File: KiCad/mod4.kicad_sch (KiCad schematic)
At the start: 51 parts, among them M7 Fan_4pin, M8 Fan_4pin, U4 ZD25Q64BSIGT

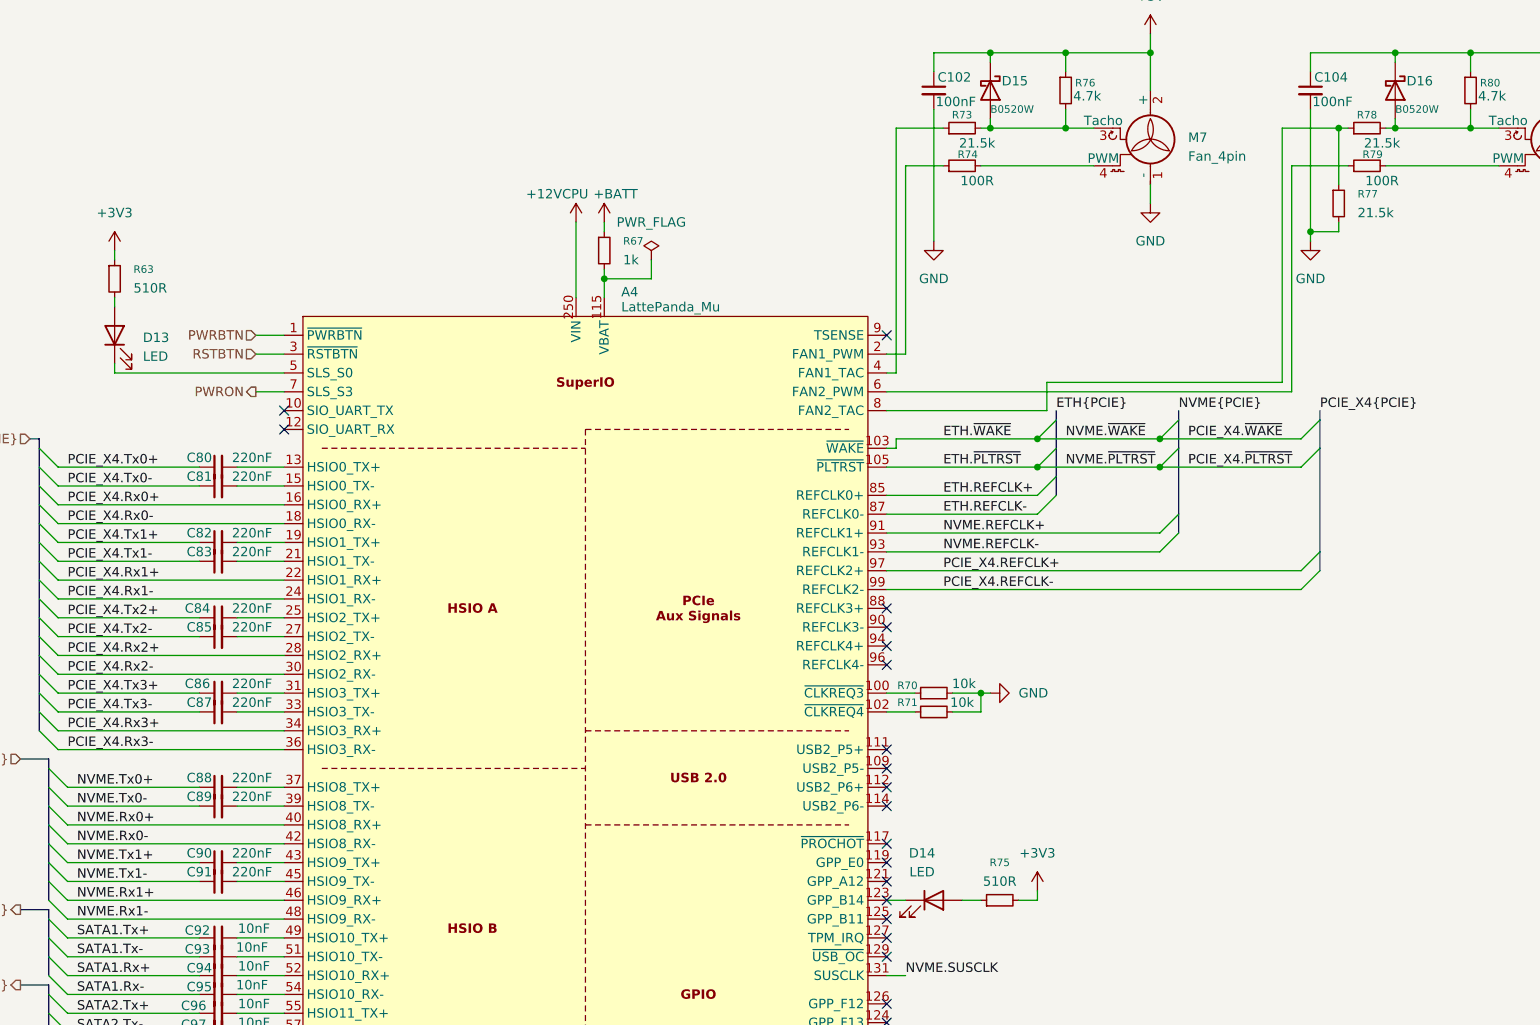
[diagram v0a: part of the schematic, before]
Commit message: Add most passive component footprints
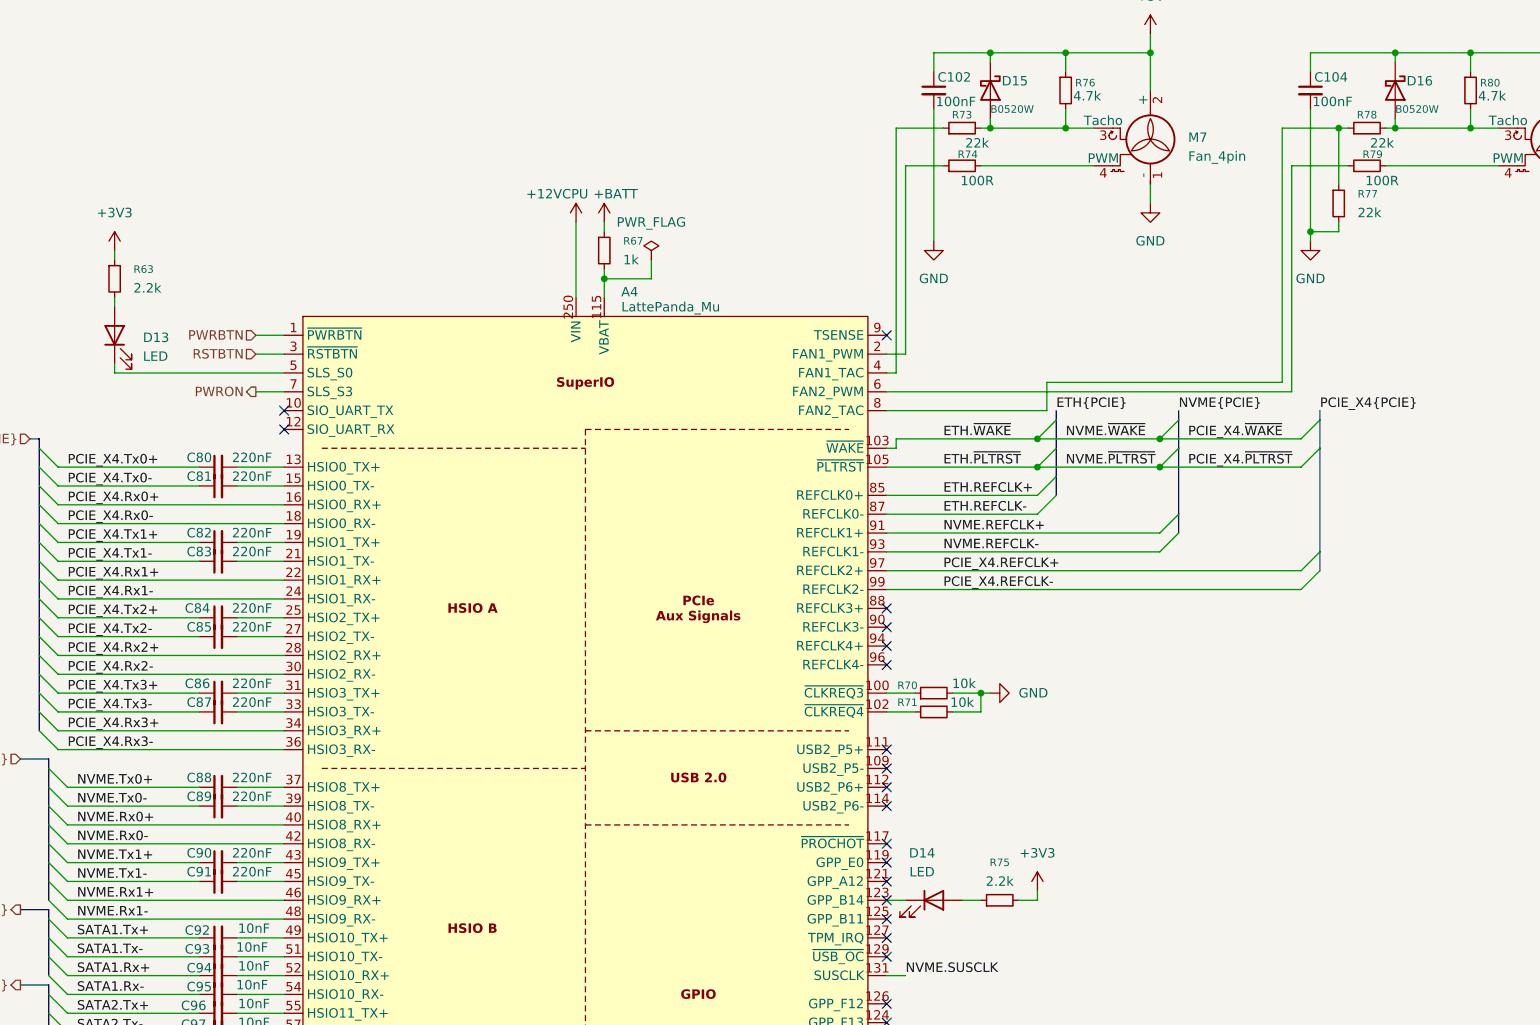
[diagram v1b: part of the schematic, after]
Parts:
- C100, C101, C102, C103, C104, C80, C81, C82, C83, C84, C85, C86, C87, C88, C89, C90, C91, C92, C93, C94, C95, C96, C97, C98, C99: footprint Capacitor_SMD:C_0603_1608Metric -> Capacitor_SMD:C_0402_1005Metric
- D13, D14: footprint (none) -> LED_SMD:LED_0603_1608Metric
- D15, D16: footprint (none) -> Diode_SMD:D_SOD-123
- M7, M8: footprint (none) -> Connector:FanPinHeader_1x04_P2.54mm_Vertical
- R63, R75: value 510R -> 2.2k; footprint (none) -> Resistor_SMD:R_0402_1005Metric
- R64, R65, R66, R68, R69, R70, R71, R72, R74, R76, R79, R80: footprint (none) -> Resistor_SMD:R_0402_1005Metric
- R67: footprint (none) -> Resistor_SMD:R_0805_2012Metric
- R73, R77, R78: value 21.5k -> 22k; footprint (none) -> Resistor_SMD:R_0402_1005Metric
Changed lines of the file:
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@@
 			)
 		)
-		(property "Footprint" "Capacitor_SMD:C_0603_1608Metric"
+		(property "Footprint" "Capacitor_SMD:C_0402_1005Metric"
 			(at 237.49 176.53 0)
 			(effects
@@
 			)
 		)
-		(property "Footprint" ""
+		(property "Footprint" "Resistor_SMD:R_0402_1005Metric"
 			(at 334.01 133.35 0)
 			(effects
@@
 			)
 		)
-		(property "Footprint" ""
+		(property "Footprint" "Resistor_SMD:R_0402_1005Metric"
 			(at 351.79 52.07 0)
 			(effects
@@
 			)
 		)
-		(property "Footprint" "Capacitor_SMD:C_0603_1608Metric"
+		(property "Footprint" "Capacitor_SMD:C_0402_1005Metric"
 			(at 237.49 181.61 0)
 			(effects
@@
 			)
 		)
-		(property "Footprint" ""
+		(property "Footprint" "Resistor_SMD:R_0402_1005Metric"
 			(at 237.49 232.41 0)
 			(effects
@@
 			)
 		)
-		(property "Value" "21.5k"
+		(property "Value" "22k"
 			(at 391.16 68.5799 0)
 			(effects
@@
 			)
 		)
-		(property "Footprint" ""
+		(property "Footprint" "Resistor_SMD:R_0402_1005Metric"
 			(at 388.62 67.31 0)
 			(effects
@@
 			)
 		)
-		(property "Footprint" "Capacitor_SMD:C_0603_1608Metric"
+		(property "Footprint" "Capacitor_SMD:C_0402_1005Metric"
 			(at 237.49 123.19 0)
 			(effects
@@
 			)
 		)
-		(property "Footprint" "Capacitor_SMD:C_0603_1608Metric"
+		(property "Footprint" "Capacitor_SMD:C_0402_1005Metric"
 			(at 237.49 115.57 0)
 			(effects
@@
 			)
 		)
-		(property "Footprint" ""
+		(property "Footprint" "Resistor_SMD:R_0402_1005Metric"
 			(at 406.4 52.07 0)
 			(effects
@@
 			)
 		)
-		(property "Value" "21.5k"
+		(property "Value" "22k"
 			(at 394.462 59.182 90)
 			(effects
@@
 			)
 		)
-		(property "Footprint" ""
+		(property "Footprint" "Resistor_SMD:R_0402_1005Metric"
 			(at 392.43 57.15 0)
 			(effects
@@
 			)
 		)
-		(property "Value" "21.5k"
+		(property "Value" "22k"
 			(at 339.852 59.182 90)
 			(effects
@@
 			)
 		)
-		(property "Footprint" ""
+		(property "Footprint" "Resistor_SMD:R_0402_1005Metric"
 			(at 337.82 57.15 0)
 			(effects
@@
 			)
 		)
-		(property "Footprint" "Capacitor_SMD:C_0603_1608Metric"
+		(property "Footprint" "Capacitor_SMD:C_0402_1005Metric"
 			(at 384.81 52.07 0)
 			(effects
@@
 			)
 		)
-		(property "Footprint" "Capacitor_SMD:C_0603_1608Metric"
+		(property "Footprint" "Capacitor_SMD:C_0402_1005Metric"
 			(at 237.49 168.91 0)
 			(effects
@@
 			)
 		)
-		(property "Footprint" "Capacitor_SMD:C_0603_1608Metric"
+		(property "Footprint" "Capacitor_SMD:C_0402_1005Metric"
 			(at 237.49 166.37 0)
 			(effects
@@
 			)
 		)
-		(property "Footprint" ""
+		(property "Footprint" "Connector:FanPinHeader_1x04_P2.54mm_Vertical"
 			(at 417.83 59.436 0)
 			(effects
@@
 			)
 		)
-		(property "Footprint" ""
+		(property "Footprint" "Resistor_SMD:R_0402_1005Metric"
 			(at 330.2 284.48 0)
 			(effects
@@
 			)
 		)
-		(property "Footprint" ""
+		(property "Footprint" "Resistor_SMD:R_0402_1005Metric"
 			(at 237.49 270.51 0)
 			(effects
@@
 			)
 		)
-		(property "Footprint" "Capacitor_SMD:C_0603_1608Metric"
+		(property "Footprint" "Capacitor_SMD:C_0402_1005Metric"
 			(at 237.49 191.77 0)
 			(effects
@@
 			)
 		)
-		(property "Footprint" ""
+		(property "Footprint" "Resistor_SMD:R_0805_2012Metric"
 			(at 289.56 73.66 0)
 			(effects
@@
 			)
 		)
-		(property "Footprint" ""
+		(property "Footprint" "Connector:FanPinHeader_1x04_P2.54mm_Vertical"
 			(at 363.22 59.436 0)
 			(effects
@@
 			)
 		)
-		(property "Footprint" "Capacitor_SMD:C_0603_1608Metric"
+		(property "Footprint" "Capacitor_SMD:C_0402_1005Metric"
 			(at 237.49 184.15 0)
 			(effects
@@
 			)
 		)
-		(property "Footprint" "Capacitor_SMD:C_0603_1608Metric"
+		(property "Footprint" "Capacitor_SMD:C_0402_1005Metric"
 			(at 237.49 102.87 0)
 			(effects
@@
 			)
 		)
-		(property "Footprint" "Capacitor_SMD:C_0603_1608Metric"
+		(property "Footprint" "Capacitor_SMD:C_0402_1005Metric"
 			(at 237.49 173.99 0)
 			(effects
@@
 			)
 		)
-		(property "Footprint" ""
+		(property "Footprint" "Resistor_SMD:R_0402_1005Metric"
 			(at 330.2 257.81 0)
 			(effects
@@
 			)
 		)
-		(property "Footprint" "Capacitor_SMD:C_0603_1608Metric"
+		(property "Footprint" "Capacitor_SMD:C_0402_1005Metric"
 			(at 237.49 105.41 0)
 			(effects
@@
 			)
 		)
-		(property "Footprint" ""
+		(property "Footprint" "Resistor_SMD:R_0402_1005Metric"
 			(at 335.28 257.81 0)
 			(effects
@@
 			)
 		)
-		(property "Footprint" ""
+		(property "Footprint" "LED_SMD:LED_0603_1608Metric"
 			(at 334.01 161.29 0)
 			(effects
@@
 			)
 		)
-		(property "Footprint" ""
+		(property "Footprint" "Resistor_SMD:R_0402_1005Metric"
 			(at 392.43 62.23 0)
 			(effects
@@
 			)
 		)
-		(property "Footprint" ""
+		(property "Footprint" "Resistor_SMD:R_0402_1005Metric"
 			(at 237.49 308.61 0)
 			(effects
@@
 			)
 		)
-		(property "Value" "510R"
+		(property "Value" "2.2k"
 			(at 226.06 78.7399 0)
 			(effects
@@
 			)
 		)
-		(property "Footprint" ""
+		(property "Footprint" "Resistor_SMD:R_0402_1005Metric"
 			(at 223.52 77.47 0)
 			(effects
@@
 			)
 		)
-		(property "Footprint" "Capacitor_SMD:C_0603_1608Metric"
+		(property "Footprint" "Capacitor_SMD:C_0402_1005Metric"
 			(at 237.49 171.45 0)
 			(effects
@@
 			)
 		)
-		(property "Footprint" "Capacitor_SMD:C_0603_1608Metric"
+		(property "Footprint" "Capacitor_SMD:C_0402_1005Metric"
 			(at 237.49 113.03 0)
 			(effects
@@
 			)
 		)
-		(property "Footprint" ""
+		(property "Footprint" "Resistor_SMD:R_0402_1005Metric"
 			(at 337.82 62.23 0)
 			(effects
@@
 			)
 		)
-		(property "Footprint" "Capacitor_SMD:C_0603_1608Metric"
+		(property "Footprint" "Capacitor_SMD:C_0402_1005Metric"
 			(at 237.49 158.75 0)
 			(effects
@@
 			)
 		)
-		(property "Footprint" ""
+		(property "Footprint" "Diode_SMD:D_SOD-123"
 			(at 396.24 52.07 0)
 			(effects
@@
 			)
 		)
-		(property "Footprint" ""
+		(property "Footprint" "LED_SMD:LED_0603_1608Metric"
 			(at 223.52 85.09 0)
 			(effects
@@
 			)
 		)
-		(property "Footprint" ""
+		(property "Footprint" "Resistor_SMD:R_0402_1005Metric"
 			(at 334.01 135.89 0)
 			(effects
@@
 			)
 		)
-		(property "Footprint" "Capacitor_SMD:C_0603_1608Metric"
+		(property "Footprint" "Capacitor_SMD:C_0402_1005Metric"
 			(at 237.49 179.07 0)
 			(effects
@@
 			)
 		)
-		(property "Footprint" "Capacitor_SMD:C_0603_1608Metric"
+		(property "Footprint" "Capacitor_SMD:C_0402_1005Metric"
 			(at 237.49 189.23 0)
 			(effects
@@
 			)
 		)
-		(property "Value" "510R"
+		(property "Value" "2.2k"
 			(at 342.9 158.75 90)
 			(effects
@@
 			)
 		)
-		(property "Footprint" ""
+		(property "Footprint" "Resistor_SMD:R_0402_1005Metric"
 			(at 342.9 161.29 0)
 			(effects
@@
 			)
 		)
-		(property "Footprint" "Capacitor_SMD:C_0603_1608Metric"
+		(property "Footprint" "Capacitor_SMD:C_0402_1005Metric"
 			(at 237.49 156.21 0)
 			(effects
@@
 			)
 		)
-		(property "Footprint" "Capacitor_SMD:C_0603_1608Metric"
+		(property "Footprint" "Capacitor_SMD:C_0402_1005Metric"
 			(at 334.01 52.07 0)
 			(effects
@@
 			)
 		)
-		(property "Footprint" "Capacitor_SMD:C_0603_1608Metric"
+		(property "Footprint" "Capacitor_SMD:C_0402_1005Metric"
 			(at 353.06 254 0)
 			(effects
@@
 			)
 		)
-		(property "Footprint" "Capacitor_SMD:C_0603_1608Metric"
+		(property "Footprint" "Capacitor_SMD:C_0402_1005Metric"
 			(at 237.49 125.73 0)
 			(effects
@@
 			)
 		)
-		(property "Footprint" "Capacitor_SMD:C_0603_1608Metric"
+		(property "Footprint" "Capacitor_SMD:C_0402_1005Metric"
 			(at 237.49 148.59 0)
 			(effects
@@
 			)
 		)
-		(property "Footprint" "Capacitor_SMD:C_0603_1608Metric"
+		(property "Footprint" "Capacitor_SMD:C_0402_1005Metric"
 			(at 237.49 133.35 0)
 			(effects
@@
 			)
 		)
-		(property "Footprint" "Capacitor_SMD:C_0603_1608Metric"
+		(property "Footprint" "Capacitor_SMD:C_0402_1005Metric"
 			(at 237.49 135.89 0)
 			(effects
@@
 			)
 		)
-		(property "Footprint" ""
+		(property "Footprint" "Diode_SMD:D_SOD-123"
 			(at 341.63 52.07 0)
 			(effects
@@
 			)
 		)
-		(property "Footprint" "Capacitor_SMD:C_0603_1608Metric"
+		(property "Footprint" "Capacitor_SMD:C_0402_1005Metric"
 			(at 237.49 146.05 0)
 			(effects

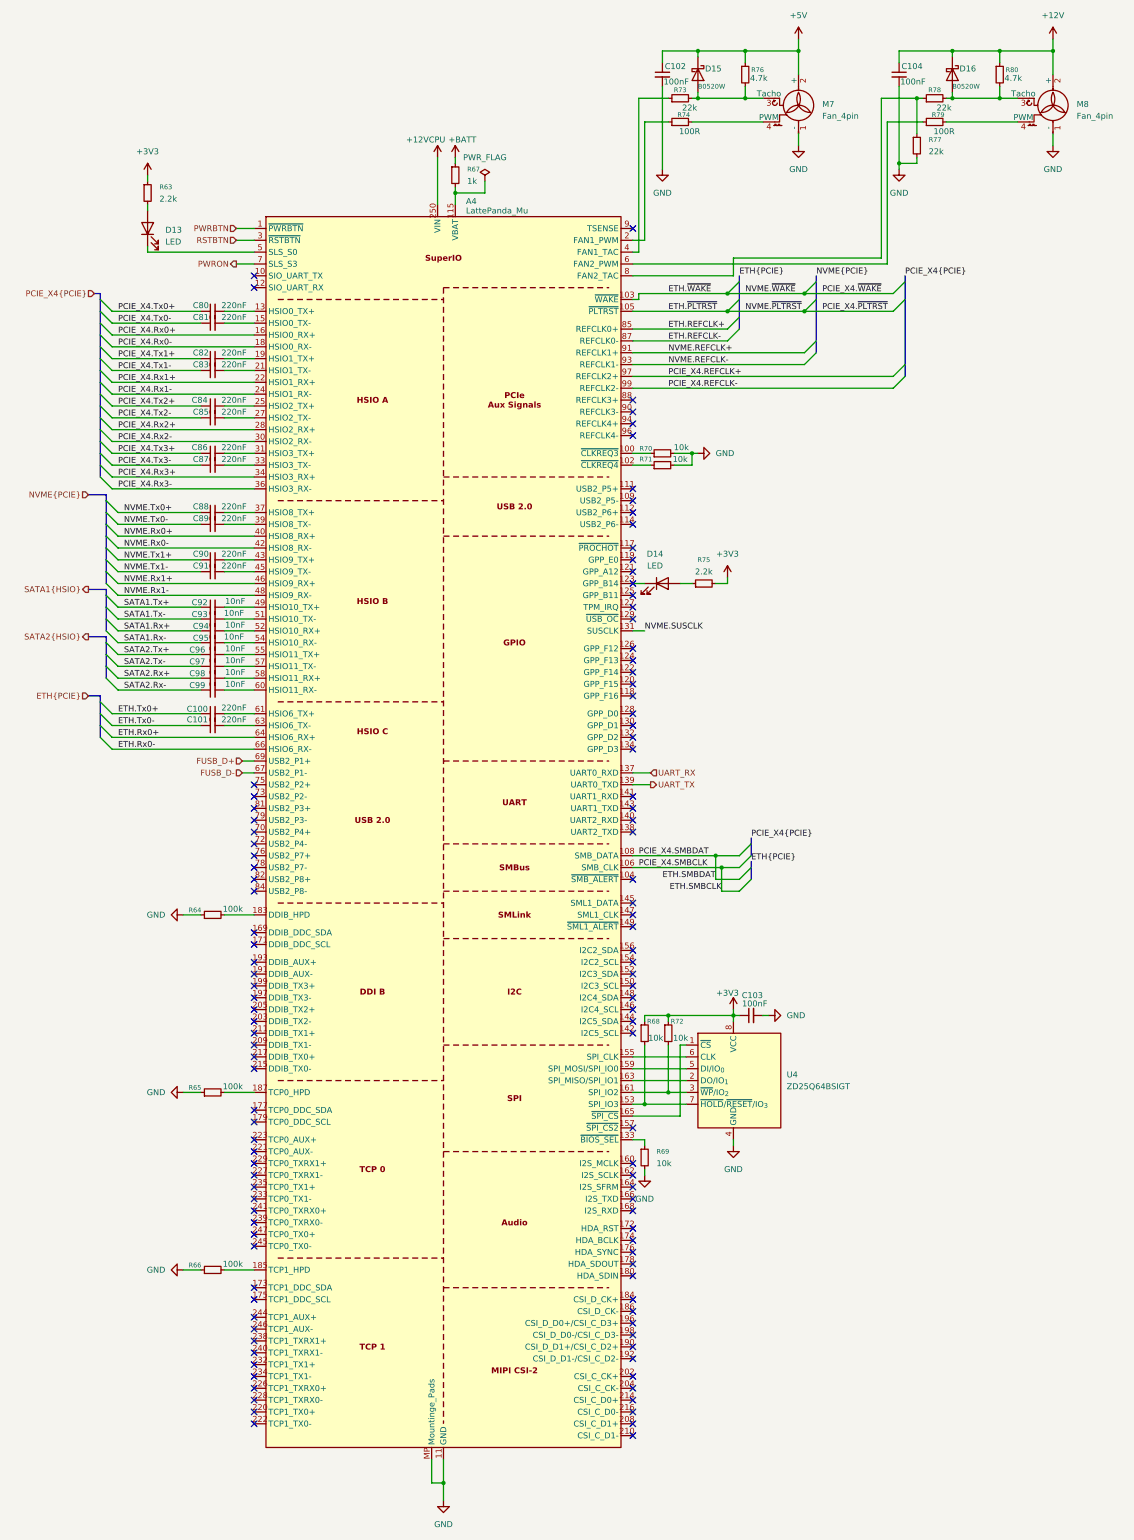
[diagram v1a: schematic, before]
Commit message: Finish fixing footprints
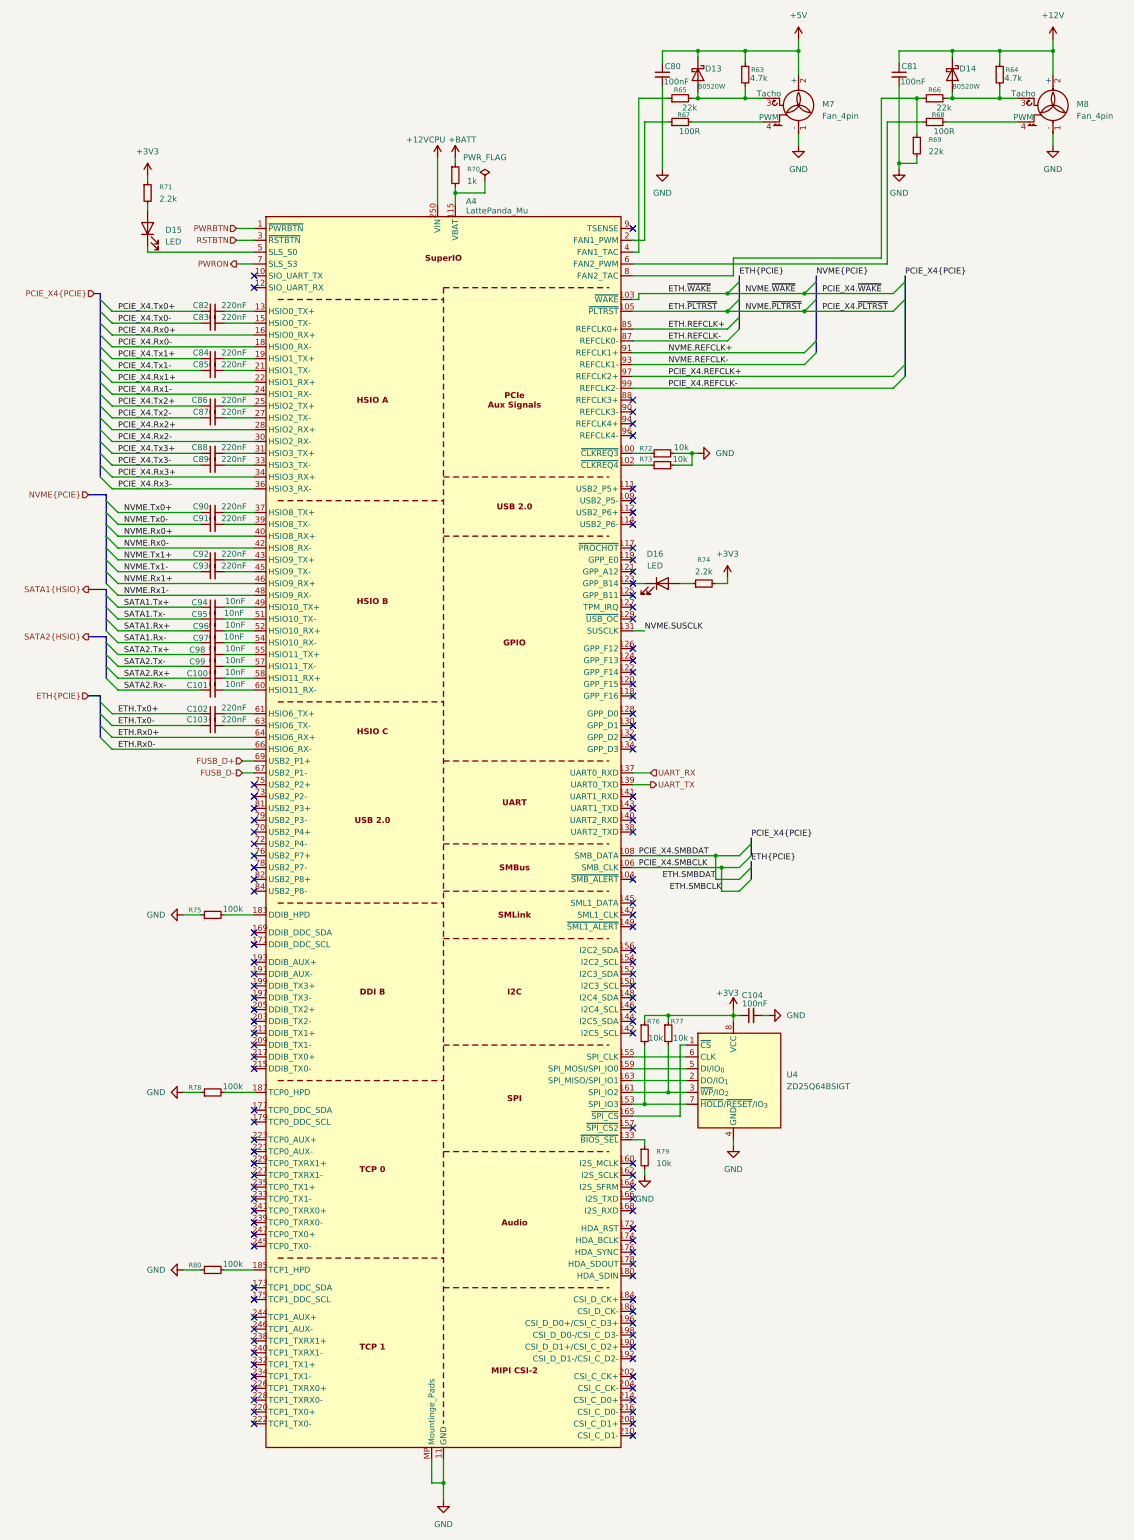
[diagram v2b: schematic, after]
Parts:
- renumbered C98 to C100, C99 to C101, C100 to C102, C101 to C103, C103 to C104, C102 to C80, C104 to C81, C80 to C82, C81 to C83, C82 to C84, C83 to C85, C84 to C86, C85 to C87, C86 to C88, C87 to C89, C88 to C90, C89 to C91, C90 to C92, C91 to C93, C92 to C94, C93 to C95, C94 to C96, C95 to C97, C96 to C98, C97 to C99, D15 to D13, D16 to D14, D13 to D15, D14 to D16, R76 to R63, R80 to R64, R73 to R65, R78 to R66, R74 to R67, R79 to R68, R77 to R69, R67 to R70, R63 to R71, R70 to R72, R71 to R73, R75 to R74, R64 to R75, R68 to R76, R72 to R77, R65 to R78, R69 to R79, R66 to R80
